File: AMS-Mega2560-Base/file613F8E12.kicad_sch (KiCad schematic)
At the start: 8 parts, among them IC18 MAX31865AAP+, J28 Conn_01x02, J29 Conn_01x03, J30 Conn_01x02

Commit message: continuing pcb layout
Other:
- note added: "100nF for 100 ohm RTD, 10nF for 1K for Cap between RTDIN- and RTDIN+"
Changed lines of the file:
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@@
     (stroke (width 0) (type default) (color 0 0 0 0))
   )
-  (label "2-3" (at 196.85 99.06 0)
+  (text "100nF for 100 ohm RTD, 10nF for 1K\nfor Cap between RTDIN- and RTDIN+"
+    (at 137.795 109.855 0)
+    (effects (font (size 1.25 1.25)) (justify left bottom))
+  )
+  (label "2-3" (at 194.31 99.695 0)
     (effects (font (size 1.27 1.27)) (justify left bottom))
   )
@@
     (effects (font (size 1.27 1.27)) (justify left bottom))
   )
-  (label "2-4" (at 91.44 111.76 0)
+  (label "2-4" (at 92.075 112.395 0)
     (effects (font (size 1.27 1.27)) (justify left bottom))
   )
-  (label "3" (at 93.98 107.95 0)
+  (label "3" (at 94.615 107.315 0)
     (effects (font (size 1.27 1.27)) (justify left bottom))
   )

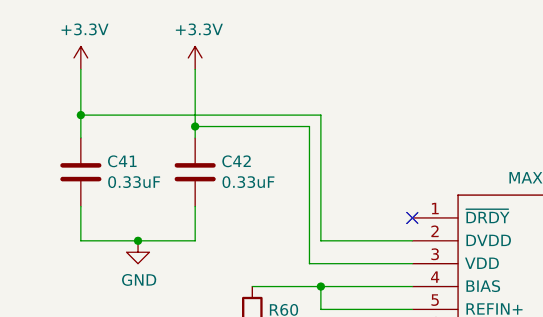
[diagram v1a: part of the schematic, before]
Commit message: WIP for power on input and RTC battery switch over.
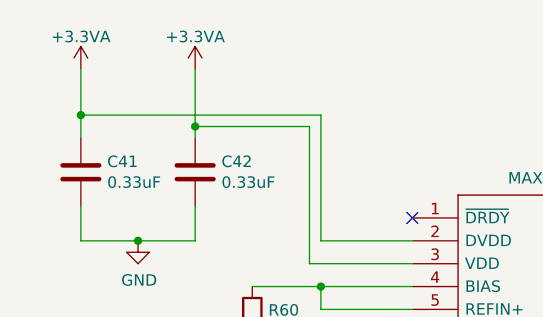
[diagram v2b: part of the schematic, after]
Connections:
- net +3V3 renamed +3.3VA
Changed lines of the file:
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@@
-    (pin "1")
-  )
-  (symbol (lib_id "power:+3.3V") (at 99.06 60.96 0)
-    (in_bom yes) (on_board yes)
-    (property "Reference" "#PWR0120" (id 0) (at 99.06 64.77 0)
-      (effects (font (size 1.27 1.27)) hide)
-    )
-    (property "Value" "+3.3V" (id 1) (at 99.441 56.5658 0))
-    (property "Footprint" "" (id 2) (at 99.06 60.96 0)
-      (effects (font (size 1.27 1.27)) hide)
-    )
-    (property "Datasheet" "" (id 3) (at 99.06 60.96 0)
-      (effects (font (size 1.27 1.27)) hide)
-    )
     (pin "1")
   )
@@
     (pin "1")
   )
-  (symbol (lib_id "power:+3.3V") (at 111.76 60.96 0)
-    (in_bom yes) (on_board yes)
-    (property "Reference" "#PWR0123" (id 0) (at 111.76 64.77 0)
-      (effects (font (size 1.27 1.27)) hide)
-    )
-    (property "Value" "+3.3V" (id 1) (at 112.141 56.5658 0))
-    (property "Footprint" "" (id 2) (at 111.76 60.96 0)
-      (effects (font (size 1.27 1.27)) hide)
-    )
-    (property "Datasheet" "" (id 3) (at 111.76 60.96 0)
-      (effects (font (size 1.27 1.27)) hide)
-    )
-    (pin "1")
-  )
   (symbol (lib_id "Connector_Generic:Conn_01x02") (at 97.79 95.25 0) (mirror y)
     (in_bom yes) (on_board yes)
@@
     (pin "2")
   )
+  (symbol (lib_id "power:+3.3VA") (at 111.76 60.96 0)
+    (in_bom yes) (on_board yes) (fields_autoplaced)
+    (property "Reference" "#PWR0134" (id 0) (at 111.76 64.77 0)
+      (effects (font (size 1.27 1.27)) hide)
+    )
+    (property "Value" "+3.3VA" (id 1) (at 111.76 57.3555 0))
+    (property "Footprint" "" (id 2) (at 111.76 60.96 0)
+      (effects (font (size 1.27 1.27)) hide)
+    )
+    (property "Datasheet" "" (id 3) (at 111.76 60.96 0)
+      (effects (font (size 1.27 1.27)) hide)
+    )
+    (pin "1")
+  )
+  (symbol (lib_id "power:+3.3VA") (at 99.06 60.96 0)
+    (in_bom yes) (on_board yes) (fields_autoplaced)
+    (property "Reference" "#PWR0130" (id 0) (at 99.06 64.77 0)
+      (effects (font (size 1.27 1.27)) hide)
+    )
+    (property "Value" "+3.3VA" (id 1) (at 99.06 57.3555 0))
+    (property "Footprint" "" (id 2) (at 99.06 60.96 0)
+      (effects (font (size 1.27 1.27)) hide)
+    )
+    (property "Datasheet" "" (id 3) (at 99.06 60.96 0)
+      (effects (font (size 1.27 1.27)) hide)
+    )
+    (pin "1")
+  )
 )

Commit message: still fixing ERC stuff
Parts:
- renumbered C41 to C1, C42 to C2, C43 to C3, IC18 to IC3, J29 to J10, J30 to J11, J28 to J9, R60 to R2
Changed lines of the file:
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@@
   (symbol (lib_id "SamacSys_Parts:MAX31865AAP+") (at 135.89 77.47 0)
     (in_bom yes) (on_board yes)
-    (property "Reference" "IC18" (id 0) (at 153.67 70.739 0))
+    (property "Reference" "IC3" (id 0) (at 153.67 70.739 0))
     (property "Value" "MAX31865AAP+" (id 1) (at 153.67 73.0504 0))
     (property "Footprint" "SamacSys_Parts:SOP65P778X199-20N" (id 2) (at 167.64 74.93 0)
@@
   (symbol (lib_id "power:GND") (at 194.31 80.01 0)
     (in_bom yes) (on_board yes)
-    (property "Reference" "#PWR0124" (id 0) (at 194.31 86.36 0)
+    (property "Reference" "#PWR026" (id 0) (at 194.31 86.36 0)
       (effects (font (size 1.27 1.27)) hide)
     )
@@
   (symbol (lib_id "Device:C") (at 111.76 72.39 0)
     (in_bom yes) (on_board yes)
-    (property "Reference" "C42" (id 0) (at 114.681 71.2216 0)
+    (property "Reference" "C2" (id 0) (at 114.681 71.2216 0)
       (effects (font (size 1.27 1.27)) (justify left))
     )
@@
   (symbol (lib_id "Device:C") (at 99.06 72.39 0)
     (in_bom yes) (on_board yes)
-    (property "Reference" "C41" (id 0) (at 101.981 71.2216 0)
+    (property "Reference" "C1" (id 0) (at 101.981 71.2216 0)
       (effects (font (size 1.27 1.27)) (justify left))
     )
@@
   (symbol (lib_id "power:GND") (at 105.41 80.01 0)
     (in_bom yes) (on_board yes)
-    (property "Reference" "#PWR0122" (id 0) (at 105.41 86.36 0)
+    (property "Reference" "#PWR024" (id 0) (at 105.41 86.36 0)
       (effects (font (size 1.27 1.27)) hide)
     )
@@
   (symbol (lib_id "Device:R") (at 118.11 88.9 0)
     (in_bom yes) (on_board yes)
-    (property "Reference" "R60" (id 0) (at 119.888 87.7316 0)
+    (property "Reference" "R2" (id 0) (at 119.888 87.7316 0)
       (effects (font (size 1.27 1.27)) (justify left))
     )
@@
   (symbol (lib_id "power:GND") (at 104.14 113.03 0)
     (in_bom yes) (on_board yes)
-    (property "Reference" "#PWR0121" (id 0) (at 104.14 119.38 0)
+    (property "Reference" "#PWR023" (id 0) (at 104.14 119.38 0)
       (effects (font (size 1.27 1.27)) hide)
     )
@@
   (symbol (lib_id "Connector_Generic:Conn_01x02") (at 97.79 95.25 0) (mirror y)
     (in_bom yes) (on_board yes)
-    (property "Reference" "J28" (id 0) (at 99.8728 89.7382 0))
+    (property "Reference" "J9" (id 0) (at 99.8728 89.7382 0))
     (property "Value" "Conn_01x02" (id 1) (at 99.8728 92.0496 0))
     (property "Footprint" "Connector_PinHeader_2.54mm:PinHeader_1x02_P2.54mm_Vertical" (id 2) (at 97.79 95.25 0)
@@
   (symbol (lib_id "Connector_Generic:Conn_01x03") (at 97.79 109.22 0) (mirror y)
     (in_bom yes) (on_board yes)
-    (property "Reference" "J29" (id 0) (at 99.8728 101.1682 0))
+    (property "Reference" "J10" (id 0) (at 99.8728 101.1682 0))
     (property "Value" "Conn_01x03" (id 1) (at 99.8728 103.4796 0))
     (property "Footprint" "Connector_PinHeader_2.54mm:PinHeader_1x03_P2.54mm_Vertical" (id 2) (at 97.79 109.22 0)
@@
   (symbol (lib_id "Connector_Generic:Conn_01x02") (at 191.77 97.79 0)
     (in_bom yes) (on_board yes)
-    (property "Reference" "J30" (id 0) (at 193.802 97.9932 0)
+    (property "Reference" "J11" (id 0) (at 193.802 97.9932 0)
       (effects (font (size 1.27 1.27)) (justify left))
     )
@@
   (symbol (lib_id "Device:C") (at 156.21 114.3 0)
     (in_bom yes) (on_board yes)
-    (property "Reference" "C43" (id 0) (at 159.131 113.1316 0)
+    (property "Reference" "C3" (id 0) (at 159.131 113.1316 0)
       (effects (font (size 1.27 1.27)) (justify left))
     )
@@
   (symbol (lib_id "power:+3.3VA") (at 111.76 60.96 0)
     (in_bom yes) (on_board yes) (fields_autoplaced)
-    (property "Reference" "#PWR0134" (id 0) (at 111.76 64.77 0)
+    (property "Reference" "#PWR025" (id 0) (at 111.76 64.77 0)
       (effects (font (size 1.27 1.27)) hide)
     )
@@
   (symbol (lib_id "power:+3.3VA") (at 99.06 60.96 0)
     (in_bom yes) (on_board yes) (fields_autoplaced)
-    (property "Reference" "#PWR0130" (id 0) (at 99.06 64.77 0)
-      (effects (font (size 1.27 1.27)) hide)
-    )
+    (property "Reference" "#PWR022" (id 0) (at 99.06 64.77 0)
+      (effects (font (size 1.27 1.27)) hide)
+    )

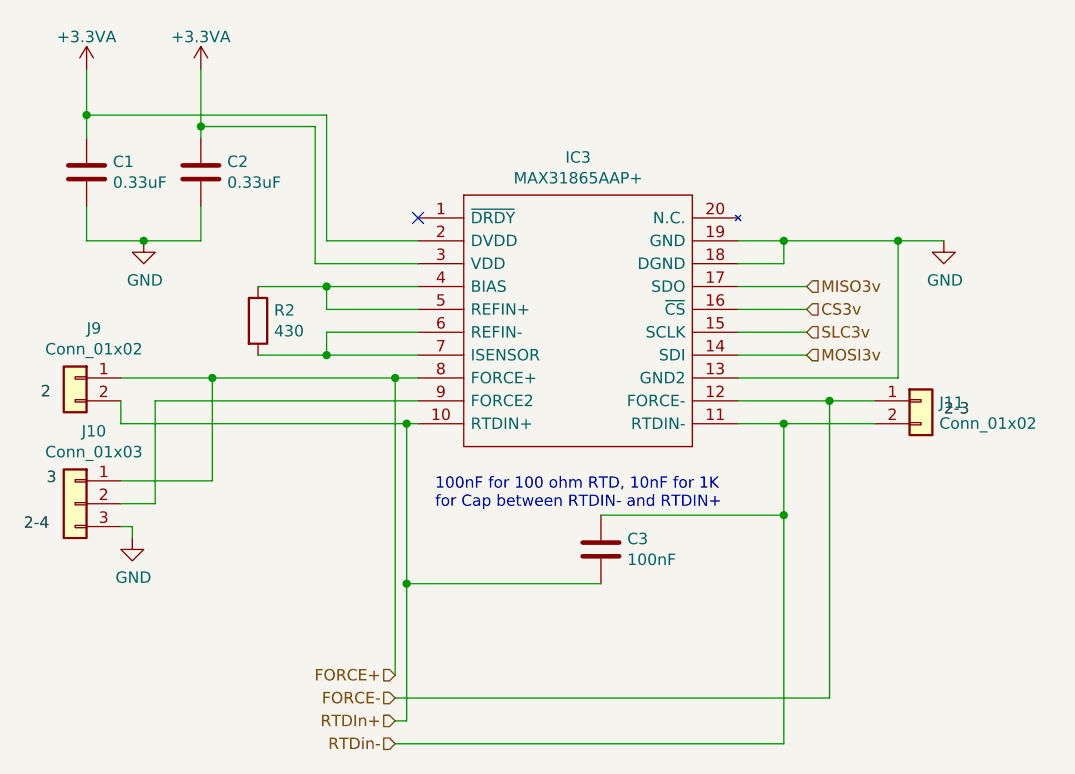
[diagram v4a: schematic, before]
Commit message: cleared all of the ERC stuff need to go over some of the power stuff for this before finishing routing.
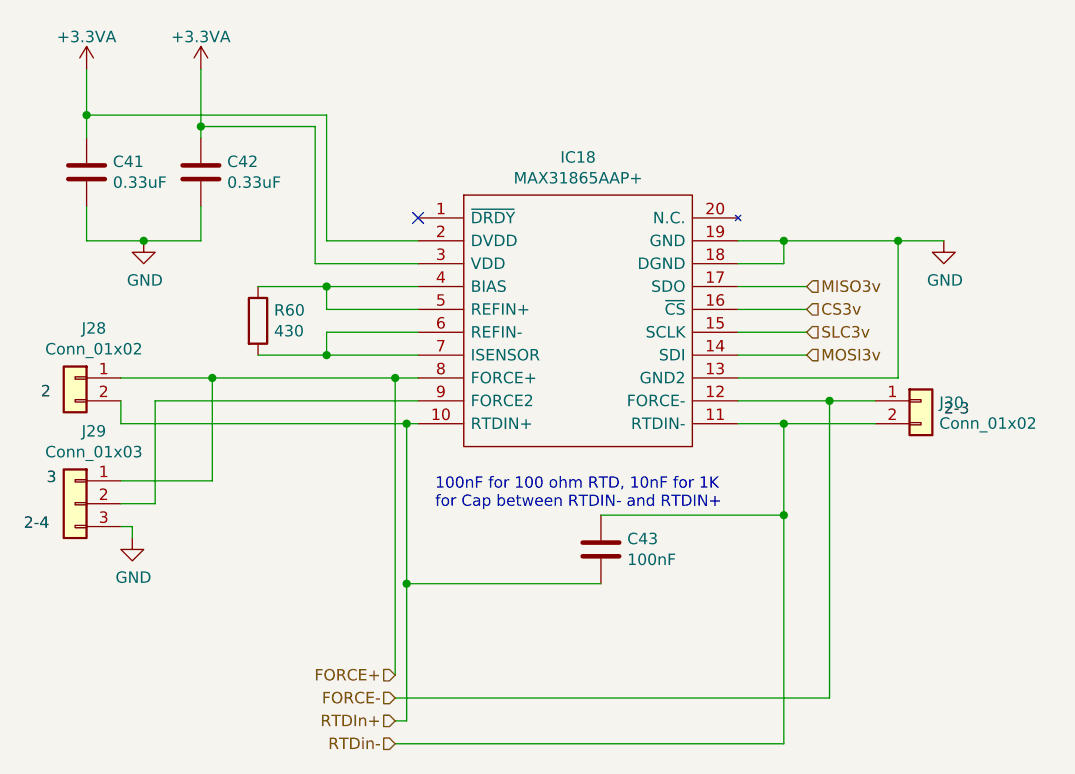
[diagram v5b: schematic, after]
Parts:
- renumbered C1 to C41, C2 to C42, C3 to C43, IC3 to IC18, J9 to J28, J10 to J29, J11 to J30, R2 to R60
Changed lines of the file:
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@@
   (symbol (lib_id "SamacSys_Parts:MAX31865AAP+") (at 135.89 77.47 0)
     (in_bom yes) (on_board yes)
-    (property "Reference" "IC3" (id 0) (at 153.67 70.739 0))
+    (property "Reference" "IC18" (id 0) (at 153.67 70.739 0))
     (property "Value" "MAX31865AAP+" (id 1) (at 153.67 73.0504 0))
     (property "Footprint" "SamacSys_Parts:SOP65P778X199-20N" (id 2) (at 167.64 74.93 0)
@@
   (symbol (lib_id "power:GND") (at 194.31 80.01 0)
     (in_bom yes) (on_board yes)
-    (property "Reference" "#PWR026" (id 0) (at 194.31 86.36 0)
+    (property "Reference" "#PWR0124" (id 0) (at 194.31 86.36 0)
       (effects (font (size 1.27 1.27)) hide)
     )
@@
   (symbol (lib_id "Device:C") (at 111.76 72.39 0)
     (in_bom yes) (on_board yes)
-    (property "Reference" "C2" (id 0) (at 114.681 71.2216 0)
+    (property "Reference" "C42" (id 0) (at 114.681 71.2216 0)
       (effects (font (size 1.27 1.27)) (justify left))
     )
@@
   (symbol (lib_id "Device:C") (at 99.06 72.39 0)
     (in_bom yes) (on_board yes)
-    (property "Reference" "C1" (id 0) (at 101.981 71.2216 0)
+    (property "Reference" "C41" (id 0) (at 101.981 71.2216 0)
       (effects (font (size 1.27 1.27)) (justify left))
     )
@@
   (symbol (lib_id "power:GND") (at 105.41 80.01 0)
     (in_bom yes) (on_board yes)
-    (property "Reference" "#PWR024" (id 0) (at 105.41 86.36 0)
+    (property "Reference" "#PWR0122" (id 0) (at 105.41 86.36 0)
       (effects (font (size 1.27 1.27)) hide)
     )
@@
   (symbol (lib_id "Device:R") (at 118.11 88.9 0)
     (in_bom yes) (on_board yes)
-    (property "Reference" "R2" (id 0) (at 119.888 87.7316 0)
+    (property "Reference" "R60" (id 0) (at 119.888 87.7316 0)
       (effects (font (size 1.27 1.27)) (justify left))
     )
@@
   (symbol (lib_id "power:GND") (at 104.14 113.03 0)
     (in_bom yes) (on_board yes)
-    (property "Reference" "#PWR023" (id 0) (at 104.14 119.38 0)
+    (property "Reference" "#PWR0121" (id 0) (at 104.14 119.38 0)
       (effects (font (size 1.27 1.27)) hide)
     )
@@
   (symbol (lib_id "Connector_Generic:Conn_01x02") (at 97.79 95.25 0) (mirror y)
     (in_bom yes) (on_board yes)
-    (property "Reference" "J9" (id 0) (at 99.8728 89.7382 0))
+    (property "Reference" "J28" (id 0) (at 99.8728 89.7382 0))
     (property "Value" "Conn_01x02" (id 1) (at 99.8728 92.0496 0))
     (property "Footprint" "Connector_PinHeader_2.54mm:PinHeader_1x02_P2.54mm_Vertical" (id 2) (at 97.79 95.25 0)
@@
   (symbol (lib_id "Connector_Generic:Conn_01x03") (at 97.79 109.22 0) (mirror y)
     (in_bom yes) (on_board yes)
-    (property "Reference" "J10" (id 0) (at 99.8728 101.1682 0))
+    (property "Reference" "J29" (id 0) (at 99.8728 101.1682 0))
     (property "Value" "Conn_01x03" (id 1) (at 99.8728 103.4796 0))
     (property "Footprint" "Connector_PinHeader_2.54mm:PinHeader_1x03_P2.54mm_Vertical" (id 2) (at 97.79 109.22 0)
@@
   (symbol (lib_id "Connector_Generic:Conn_01x02") (at 191.77 97.79 0)
     (in_bom yes) (on_board yes)
-    (property "Reference" "J11" (id 0) (at 193.802 97.9932 0)
+    (property "Reference" "J30" (id 0) (at 193.802 97.9932 0)
       (effects (font (size 1.27 1.27)) (justify left))
     )
@@
   (symbol (lib_id "Device:C") (at 156.21 114.3 0)
     (in_bom yes) (on_board yes)
-    (property "Reference" "C3" (id 0) (at 159.131 113.1316 0)
+    (property "Reference" "C43" (id 0) (at 159.131 113.1316 0)
       (effects (font (size 1.27 1.27)) (justify left))
     )
@@
   (symbol (lib_id "power:+3.3VA") (at 111.76 60.96 0)
     (in_bom yes) (on_board yes) (fields_autoplaced)
-    (property "Reference" "#PWR025" (id 0) (at 111.76 64.77 0)
+    (property "Reference" "#PWR0134" (id 0) (at 111.76 64.77 0)
       (effects (font (size 1.27 1.27)) hide)
     )
@@
   (symbol (lib_id "power:+3.3VA") (at 99.06 60.96 0)
     (in_bom yes) (on_board yes) (fields_autoplaced)
-    (property "Reference" "#PWR022" (id 0) (at 99.06 64.77 0)
-      (effects (font (size 1.27 1.27)) hide)
-    )
+    (property "Reference" "#PWR0130" (id 0) (at 99.06 64.77 0)
+      (effects (font (size 1.27 1.27)) hide)
+    )
